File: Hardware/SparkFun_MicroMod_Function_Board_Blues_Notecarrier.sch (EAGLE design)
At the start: 3 parts, among them J1 MICROMOD_FUNCTION_STANDARD, U1 NOTECARD

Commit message: Board nearly complete, nearing readiness for design review.
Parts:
- added ANT_PWR, WP: JUMPER-SMT_2_NO_SILK, SparkFun-Jumpers:JUMPER-SMT_2_NO_SILK
- added AUX_EN_LED, USB_SHLD, VIO_LED, VMODEM_LED: JUMPER-SMT_2_NC_TRACE_SILK, SparkFun-Jumpers:JUMPER-SMT_2_NC_TRACE_SILK
- added C1, C5, C6, C7: 0.1uF, SparkFun-Capacitors:0.1UF-0402T-16V-10%
- added C2: 10uF, SparkFun-Capacitors:10UF-0805-10V-10%
- added C3, C4: 100uF, SparkFun-Capacitors:100UF-POLAR-25V-20%(ELEC)
- added C8: 1.0uF, SparkFun-Capacitors:1.0UF-0402T-16V-10%
- added D1, D2: RED, SparkFun-LED:LED-RED0603
- added D3: BLUE, SparkFun-LED:LED-BLUE0603
- added D4: PRTR5V0U2F, SparkFun-IC-Power:PRTR5V0U2F
- added D5, D6: 3A/10V/280mV, SparkFun-DiscreteSemi:DIODE-SCHOTTKY-BAT60A
- added D7: 0.5A/40V/420mV, SparkFun-DiscreteSemi:DIODE-SCHOTTKY-PMEG4005EJ
- added FD1, FD2, FD3, FD4: FIDUCIALUFIDUCIAL, SparkFun-Aesthetics:FIDUCIALUFIDUCIAL
- added H1: STAND-OFF-REFLOW-M2.5_2.5MM_TALL, SparkFun-Hardware:STAND-OFF-REFLOW-M2.5_2.5MM_TALL
- added J2: MICROMOD_FUNCTION_STANDARD, SparkFun-MicroMod:MICROMOD_FUNCTION_STANDARD
- added J3: (no value), SparkFun-Connectors:CONN_01PTH_NO_SILK_YES_STOP
- added J4: (no value), SparkFun-Connectors:CONN_07NO_SILK
- added J5: (no value), SparkFun-Connectors:SIMHOLDER-NANOSIM-MOLEX
- added J6: NOTECARD, SparkFun_MicroMod_Function_Board_Blues_Notecarrier:NOTECARD
- added LOGO1: SFE_LOGO_NAME_FLAME.1_INCH, SparkFun-Aesthetics:SFE_LOGO_NAME_FLAME.1_INCH
- added LOGO2: SPECIAL_INSTRUCTIONS-ORDERING, SparkFun-Aesthetics:SPECIAL_INSTRUCTIONS-ORDERING
- added LOGO3: OSHW-LOGOMINI, SparkFun-Aesthetics:OSHW-LOGOMINI
- added MEAS: JUMPER-COMBO_2_NC_TRACE, SparkFun-Jumpers:JUMPER-COMBO_2_NC_TRACE
- added Q1, Q3: 5.8A/30V/35mΩ, SparkFun-DiscreteSemi:MOSFET-NCH-AO3404A
- added Q2, Q4: 20V/4.2A/52mΩ/1.4W, SparkFun-DiscreteSemi:MOSFET_PCH-DMG2305UX-7
- added R1, R2: 1k, SparkFun-Resistors:1KOHM-0402T-1/16W-1%
- added R10, R11, R13, R5, R7, R9: 10k, SparkFun-Resistors:10KOHM-0402T-1/16W-1%
- added R12: 2.2M, SparkFun-Resistors:2.2MOHMS-0402T-1/10W-1%
- added R3, R4: 5.1k, SparkFun-Resistors:5.1KOHM-0402T-1/16W-1%
- added R6: 4.7k, SparkFun-Resistors:4.7KOHM-0402T-1/16W-1%
- added R8: 560Ω, SparkFun-Resistors:560OHM_0402_TIGHT
- added S1: MOMENTARY-SWITCH-SPST-SMD-4.6X2.8MM, SparkFun-Switches:MOMENTARY-SWITCH-SPST-SMD-4.6X2.8MM
- added U2: TCR2EF33, SparkFun_MicroMod_Function_Board_Blues_Notecarrier:TCR2EF33
- J1: value MICROMOD_FUNCTION_STANDARD -> (none); device SparkFun-MicroMod:MICROMOD_FUNCTION_STANDARD -> SparkFun-Connectors:USB_C_2-LAYER_PADS
- U1: value NOTECARD -> EEPROM; device SparkFun_MicroMod_Function_Board_Blues_Notecarrier:NOTECARD -> SparkFun-IC-Memory:EEPROM-I2C512K
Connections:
- new net !RESET!: J3.1, J6.!RST!, S1.2
- new net 3.3V: C1.1, C7.1, D1.A, D7.C, J6.VIO, Q2.D, R10.1, R5.1, U1.VCC
- new net 3V3_IN: J2.3.3V, Q2.S, R7.1, R9.2
- new net A0: J2.EEPROM_A0, U1.A0
- new net A1: J2.EEPROM_A1, U1.A1
- new net A2: J2.EEPROM_A2, U1.A2
- new net ATTN: J2.F3, J6.ATTN
- new net AUX1/MCU_!DFU_STAT!: J2.MCU_!DFU_STAT!, J4.6, J6.AUX1
- new net AUX2: J2.F5, J4.5, J6.AUX2
- new net AUX3/MCU_!BOOT!: J2.MCU_!BOOT!, J4.4, J6.AUX3
- new net AUX4/MCU_!RST!: J2.MCU_!RST!, J4.3, J6.AUX4
- new net AUX5: J2.F6, J4.7, J6.AUX5
- new net AUX_EN: D3.A, J2.F4, J4.2, J6.AUX_EN, R10.2
- new net AUX_RX/MCU_TX: J2.MCU_DFU_TX, J6.AUX_RX
- new net AUX_TX/MCU_RX: J2.MCU_DFU_RX, J6.AUX_TX
- new net EWP: J2.EEPROM_WP, R5.2, U1.WP, WP.2
- new net GND: AUX_EN_LED.1, C1.2, C2.2, C3.-, C4.-, C5.2, C6.2, C7.2, C8.2, D4.2, H1.1, J1.GND, J2.GND, J4.1, J5.GND, J6.GND, Q1.S, Q3.S, R12.1, R3.1, R4.1, S1.1, U1.GND, U2.GND, USB_SHLD.1, VIO_LED.1, VMODEM_LED.1, WP.1
- new net N$1: J2.PWR_EN, R8.2
- new net N$10: C8.1, D7.A, U2.OUT
- new net N$11: R2.1, VMODEM_LED.2
- new net N$12: R1.1, VIO_LED.2
- new net N$13: D3.C, R6.2
- new net N$14: AUX_EN_LED.2, R6.1
- new net N$2: Q1.D, Q2.G, R9.1
- new net N$3: Q3.D, Q4.G, R11.1
- new net N$37: D5.C, D6.C, MEAS.1
- new net N$4: D1.C, R1.2
- new net N$5: R13.1, U2.EN
- new net N$6: D2.C, R2.2
- new net N$8: J1.CC2, R3.2
- new net N$9: J1.CC1, R4.2
- new net NOTECARD_RX: J2.TX, J6.RX
- new net NOTECARD_TX: J2.RX, J6.TX
- new net PWR_EN: Q1.G, Q3.G, R7.2, R8.1
- new net SCL: J2.I2C_SCL, J6.SCL, U1.SCL
- new net SDA: J2.I2C_SDA, J6.SDA, U1.SDA
- new net SHLD: J1.SHLD, USB_SHLD.2
- new net SIM_CLK: J5.CLK, J6.SIM_CLK
- new net SIM_IO: J5.I/O, J6.SIM_IO
- new net SIM_RST: J5.RST, J6.SIM_RST
- new net SIM_VCC: C2.1, J5.VCC, J6.SIM_VCC
- new net USB_IN_N: D4.3, J1.D-
- new net USB_IN_P: D4.1, J1.D+
- new net USB_N: D4.4, J6.USB_D-
- new net USB_P: D4.6, J6.USB_D+
- new net VACT_GPS_IN: ANT_PWR.2, J6.VACT_GPS_IN
- new net VACT_GPS_OUT: ANT_PWR.1, J6.V_ACT_GPS_OUT
- new net VCC: D6.A, Q4.D
- new net VCC_IN: J2.VCC, Q4.S, R11.2
- new net VIN: C3.+, C4.+, C6.1, D2.A, J6.VMODEM, MEAS.2, R12.2
- new net V_USB: C5.1, D4.5, D5.A, J1.VBUS, J6.VUSB, R13.2, U2.IN
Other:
- note added: "AUX IO Breakout"
- note added: "Blues Notecard"
- note added: "External Active Antenna Power"
- note added: "External VIO Power"
- note added: "MicroMod Function Connector"
- note added: "Power Conditioning"
- note added: "Power Control"
- note added: "Power Indication"
- note added: "Reset Button and Breakout"
- note added: "SIM Card"
- note added: "USB Input"

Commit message: Board routing complete.
Initial routing complete, now finishing silk.
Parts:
- added D8: 0.5A/40V/420mV, SparkFun-DiscreteSemi:DIODE-SCHOTTKY-PMEG4005EJ
- J4: device SparkFun-Connectors:CONN_07NO_SILK -> SparkFun-Connectors:CONN_06NO_SILK_NO_POP
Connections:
- removed net AUX5: J2.F6, J4.7, J6.AUX5
- new net N$7: D8.A, Q2.D
- net 3.3V: now also D8.C; no longer Q2.D
- net VIN: now also C5.1, R13.2, U2.IN
- net V_USB: no longer C5.1, R13.2, U2.IN

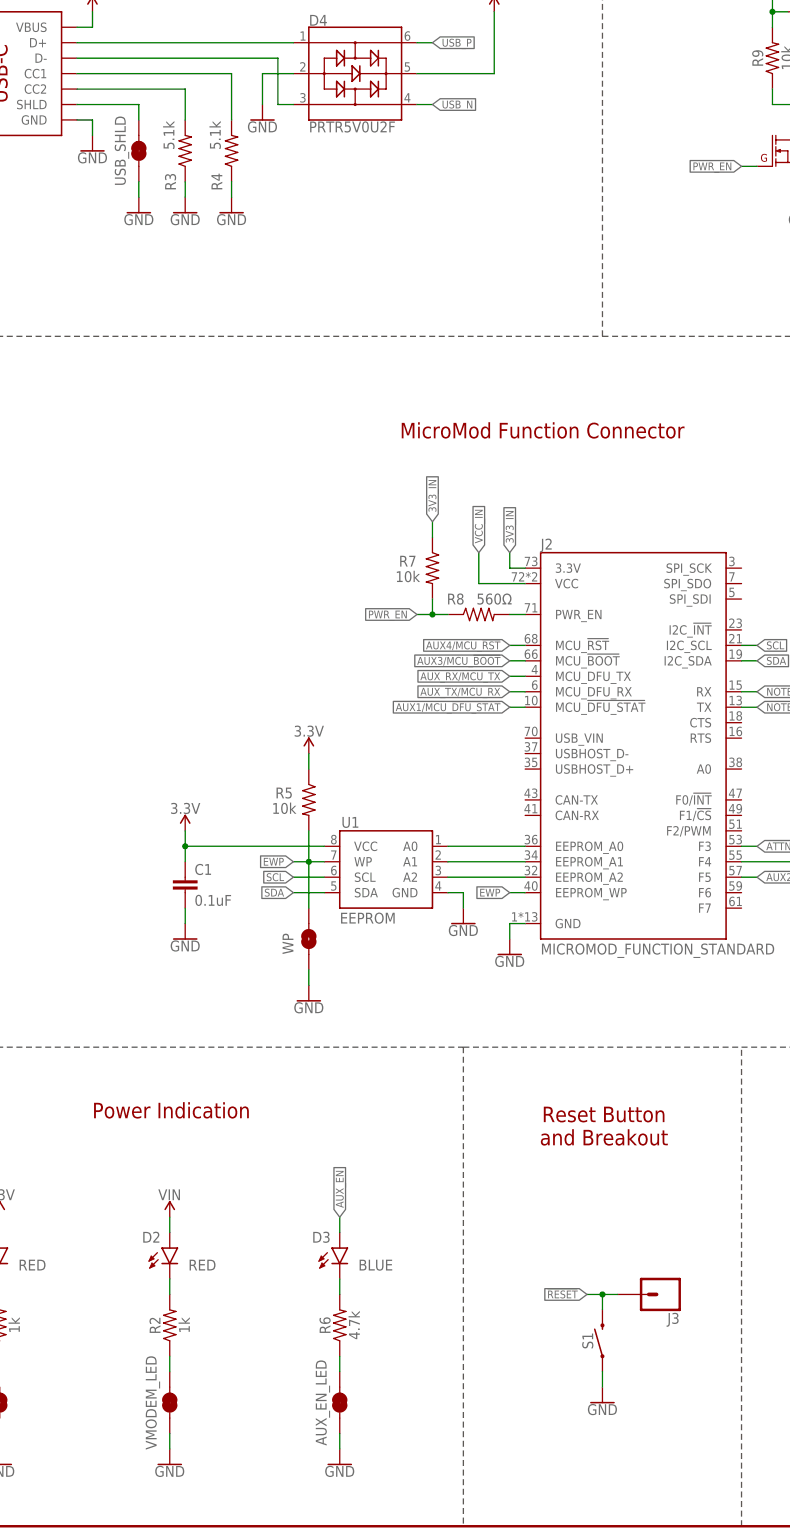
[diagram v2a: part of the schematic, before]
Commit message: Initial Silk completed.
May add Blues Wireless logo.
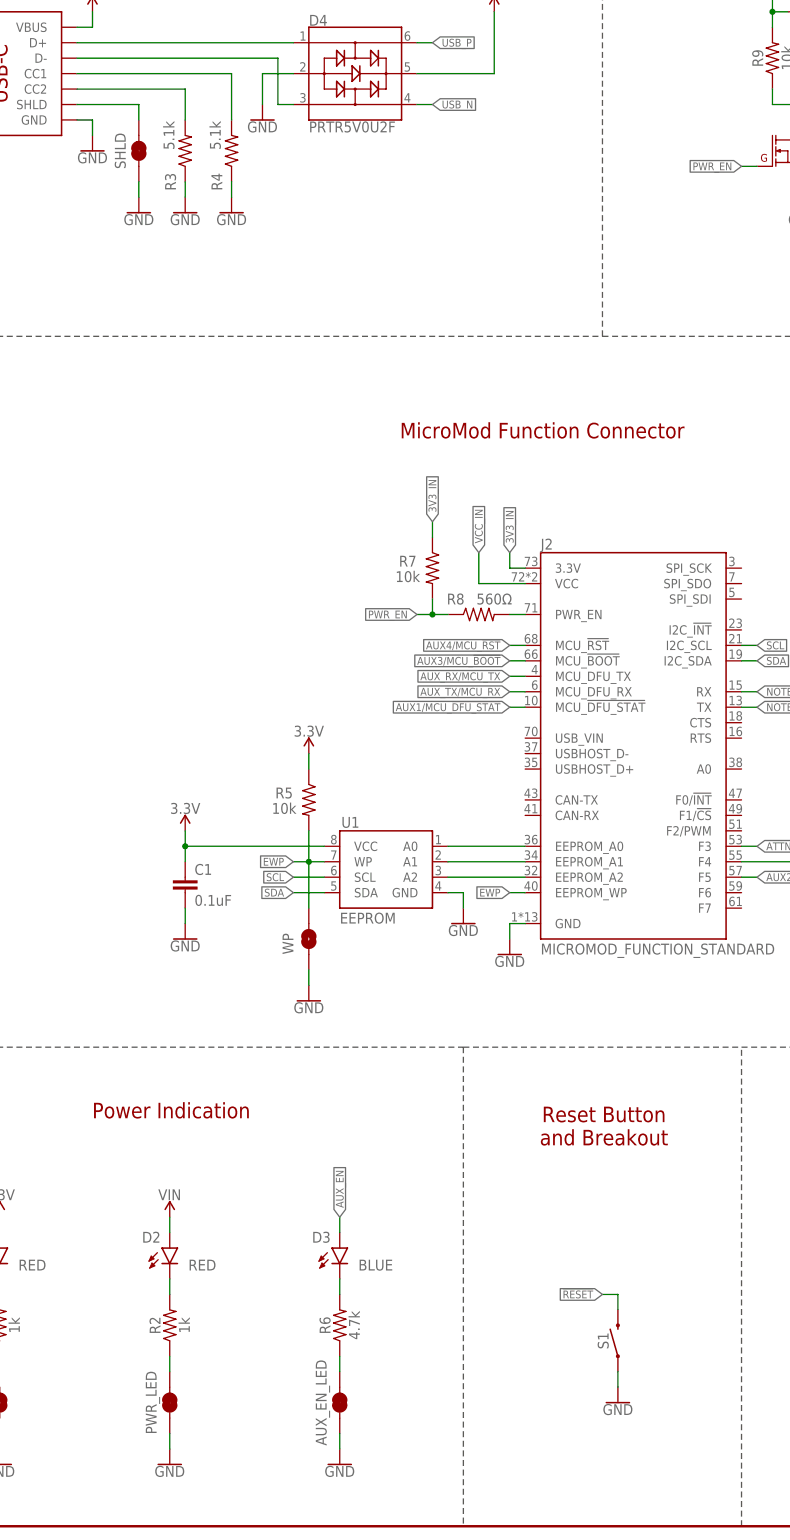
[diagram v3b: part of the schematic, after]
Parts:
- removed J3: (no value), SparkFun-Connectors:CONN_01PTH_NO_SILK_YES_STOP
- renumbered USB_SHLD to SHLD, VMODEM_LED to PWR_LED
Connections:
- net !RESET!: no longer J3.1
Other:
- moved on the sheet: S1
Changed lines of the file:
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@@
 <setting verticaltext="up"/>
 </settings>
-<grid distance="0.1" unitdist="inch" unit="inch" style="lines" multiple="1" display="no" altdistance="0.01" altunitdist="inch" altunit="inch"/>
+<grid distance="0.1" unitdist="inch" unit="inch" style="lines" multiple="1" display="yes" altdistance="0.01" altunitdist="inch" altunit="inch"/>
 <layers>
 <layer number="1" name="Top" color="4" fill="1" visible="no" active="no"/>
@@
 <part name="SUPPLY4" library="SparkFun-PowerSymbols" deviceset="V_USB" device=""/>
 <part name="SUPPLY5" library="SparkFun-PowerSymbols" deviceset="V_USB" device=""/>
-<part name="USB_SHLD" library="SparkFun-Jumpers" deviceset="JUMPER-SMT_2_NC_TRACE" device="_SILK" package3d_urn="urn:adsk.eagle:package:39281/1"/>
+<part name="SHLD" library="SparkFun-Jumpers" deviceset="JUMPER-SMT_2_NC_TRACE" device="_SILK" package3d_urn="urn:adsk.eagle:package:39281/1"/>
 <part name="R3" library="SparkFun-Resistors" deviceset="5.1KOHM" device="-0402T-1/16W-1%" value="5.1k"/>
 <part name="R4" library="SparkFun-Resistors" deviceset="5.1KOHM" device="-0402T-1/16W-1%" value="5.1k"/>
@@
 <part name="R2" library="SparkFun-Resistors" deviceset="1KOHM" device="-0402T-1/16W-1%" value="1k"/>
 <part name="VIO_LED" library="SparkFun-Jumpers" deviceset="JUMPER-SMT_2_NC_TRACE" device="_SILK" package3d_urn="urn:adsk.eagle:package:39281/1"/>
-<part name="VMODEM_LED" library="SparkFun-Jumpers" deviceset="JUMPER-SMT_2_NC_TRACE" device="_SILK" package3d_urn="urn:adsk.eagle:package:39281/1"/>
+<part name="PWR_LED" library="SparkFun-Jumpers" deviceset="JUMPER-SMT_2_NC_TRACE" device="_SILK" package3d_urn="urn:adsk.eagle:package:39281/1"/>
 <part name="GND23" library="SparkFun-PowerSymbols" deviceset="GND" device=""/>
 <part name="GND24" library="SparkFun-PowerSymbols" deviceset="GND" device=""/>
 <part name="SUPPLY16" library="SparkFun-PowerSymbols" deviceset="3.3V" device=""/>
 <part name="GND25" library="SparkFun-PowerSymbols" deviceset="GND" device=""/>
-<part name="J3" library="SparkFun-Connectors" deviceset="CONN_01" device="PTH_NO_SILK_YES_STOP"/>
 <part name="D3" library="SparkFun-LED" deviceset="LED-BLUE" device="0603" value="BLUE"/>
 <part name="R6" library="SparkFun-Resistors" deviceset="4.7KOHM" device="-0402T-1/16W-1%" value="4.7k"/>
@@
 <attribute name="VALUE" x="33.02" y="251.714" size="1.778" layer="96" font="vector" align="bottom-center"/>
 </instance>
-<instance part="USB_SHLD" gate="G$1" x="40.64" y="226.06" smashed="yes" rot="R90">
+<instance part="SHLD" gate="G$1" x="40.64" y="226.06" smashed="yes" rot="R90">
 <attribute name="NAME" x="37.592" y="226.06" size="1.778" layer="95" font="vector" rot="R90" align="center"/>
 </instance>
@@
 <attribute name="VALUE" x="208.28" y="254.254" size="1.778" layer="96" font="vector" align="bottom-center"/>
 </instance>
-<instance part="S1" gate="G$1" x="116.84" y="30.48" smashed="yes" rot="R90">
-<attribute name="NAME" x="115.316" y="30.48" size="1.778" layer="95" font="vector" rot="R90" align="bottom-center"/>
-</instance>
-<instance part="GND12" gate="1" x="116.84" y="20.32" smashed="yes">
-<attribute name="VALUE" x="116.84" y="20.066" size="1.778" layer="96" font="vector" align="top-center"/>
+<instance part="S1" gate="G$1" x="119.38" y="30.48" smashed="yes" rot="R90">
+<attribute name="NAME" x="117.856" y="30.48" size="1.778" layer="95" font="vector" rot="R90" align="bottom-center"/>
+</instance>
+<instance part="GND12" gate="1" x="119.38" y="20.32" smashed="yes">
+<attribute name="VALUE" x="119.38" y="20.066" size="1.778" layer="96" font="vector" align="top-center"/>
 </instance>
 <instance part="H1" gate="G1" x="396.24" y="132.08" smashed="yes">
@@
 <attribute name="NAME" x="14.732" y="20.32" size="1.778" layer="95" font="vector" rot="R90" align="center"/>
 </instance>
-<instance part="VMODEM_LED" gate="G$1" x="45.72" y="20.32" smashed="yes" rot="R90">
+<instance part="PWR_LED" gate="G$1" x="45.72" y="20.32" smashed="yes" rot="R90">
 <attribute name="NAME" x="42.672" y="20.32" size="1.778" layer="95" font="vector" rot="R90" align="center"/>
 </instance>
@@
 <instance part="GND25" gate="1" x="167.64" y="20.32" smashed="yes">
 <attribute name="VALUE" x="167.64" y="20.066" size="1.778" layer="96" font="vector" align="top-center"/>
-</instance>
-<instance part="J3" gate="G$1" x="127" y="38.1" smashed="yes" rot="R180">
-<attribute name="VALUE" x="129.54" y="42.926" size="1.778" layer="96" font="vector" rot="R180"/>
-<attribute name="NAME" x="129.54" y="35.052" size="1.778" layer="95" font="vector" rot="R180"/>
 </instance>
 <instance part="D3" gate="G$1" x="73.66" y="45.72" smashed="yes">
@@
 </segment>
 <segment>
-<pinref part="USB_SHLD" gate="G$1" pin="1"/>
+<pinref part="SHLD" gate="G$1" pin="1"/>
 <wire x1="40.64" y1="220.98" x2="40.64" y2="218.44" width="0.1524" layer="91"/>
 <pinref part="GND5" gate="1" pin="GND"/>
@@
 <segment>
 <pinref part="S1" gate="G$1" pin="1"/>
-<wire x1="116.84" y1="25.4" x2="116.84" y2="22.86" width="0.1524" layer="91"/>
+<wire x1="119.38" y1="25.4" x2="119.38" y2="22.86" width="0.1524" layer="91"/>
 <pinref part="GND12" gate="1" pin="GND"/>
 </segment>
@@
 </segment>
 <segment>
-<pinref part="VMODEM_LED" gate="G$1" pin="1"/>
+<pinref part="PWR_LED" gate="G$1" pin="1"/>
 <pinref part="GND24" gate="1" pin="GND"/>
 <wire x1="45.72" y1="15.24" x2="45.72" y2="12.7" width="0.1524" layer="91"/>
@@
 <wire x1="30.48" y1="233.68" x2="40.64" y2="233.68" width="0.1524" layer="91"/>
 <wire x1="40.64" y1="233.68" x2="40.64" y2="231.14" width="0.1524" layer="91"/>
-<pinref part="USB_SHLD" gate="G$1" pin="2"/>
+<pinref part="SHLD" gate="G$1" pin="2"/>
 </segment>
 </net>
@@
 <segment>
 <pinref part="S1" gate="G$1" pin="2"/>
-<wire x1="114.3" y1="38.1" x2="116.84" y2="38.1" width="0.1524" layer="91"/>
-<wire x1="116.84" y1="38.1" x2="116.84" y2="35.56" width="0.1524" layer="91"/>
 <wire x1="116.84" y1="38.1" x2="119.38" y2="38.1" width="0.1524" layer="91"/>
-<junction x="116.84" y="38.1"/>
-<label x="114.3" y="38.1" size="1.27" layer="95" font="vector" rot="R180" xref="yes"/>
-<pinref part="J3" gate="G$1" pin="1"/>
+<wire x1="119.38" y1="38.1" x2="119.38" y2="35.56" width="0.1524" layer="91"/>
+<label x="116.84" y="38.1" size="1.27" layer="95" font="vector" rot="R180" xref="yes"/>
 </segment>
 <segment>
@@
 <segment>
 <pinref part="R2" gate="G$1" pin="1"/>
-<pinref part="VMODEM_LED" gate="G$1" pin="2"/>
+<pinref part="PWR_LED" gate="G$1" pin="2"/>
 <wire x1="45.72" y1="27.94" x2="45.72" y2="25.4" width="0.1524" layer="91"/>
 </segment>

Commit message: Post DR updates.
Schematic:
Add Text to VREG
Add Text to Notecard
add 100 ohm resistor on pwr ctrl
Change Q1/Q3 transistors
Add Text to jumpers
Move V_USB on Notecard

Board:
Remove L2/L15
Add units for measures
Remove underscores from Silks
Move EWP via over
Remove copper layer notes
Give silk labels correct pointers
Increase mask stop on pads to ensure isolation
Move V_USB via down to allow ground pour
Check Wire stubs
Move 3.3V up to pour gnd better
Redo measures to make them look nice
Move some vias around to pour ground better
Place 100 ohm resistors
Place InRush current limiting resistor
Reroute
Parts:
- added R14, R15: 100, SparkFun-Resistors:100OHM-0402-TIGHT-1/16W-1%
- added R16: 1, SparkFun-Resistors:1OHM-0603-1/10W-1%
- Q1, Q3: value 5.8A/30V/35mΩ -> 220mA/50V/3.5Ω; device SparkFun-DiscreteSemi:MOSFET-NCH-AO3404A -> SparkFun-DiscreteSemi:MOSFET-NCH-BSS138
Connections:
- new net N$15: Q1.D, R14.1
- new net N$16: Q3.D, R15.1
- new net N$17: MEAS.2, R16.1
- net N$2: now also R14.2; no longer Q1.D
- net N$3: now also R15.2; no longer Q3.D
- net VIN: now also R16.2; no longer MEAS.2
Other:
- note added: "200mA out 5.5V max in"
- note added: "Connect to enable power for an active antenna. Default: Normally Open"
- note added: "Cut LED jumper to disable LED"
- note added: "Cut trace to measure current"
- note added: "USBSHLD Jumper Use this jumper to connect/disconnect your USB-C cable shield to this PCB's GND. Closed (default): connected to GND"
- note added: "VMODEM: 2.5 - 5.5V, 750mA continuous, 2A for < 20ms peak VIO: 3.3V, 150mA"
- moved on the sheet: C3, C4, C6, C7, D5, D6, H1, J6, MEAS, Q1, Q3, R12

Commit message: Update to v02.
Remove 10k PUR on AUX_EN
Add P-ch FET switch to AUX_EN
Rear Silk
Add Notecard SVG to silk
Change Title of Reset Section of Schematic
Reduce value of AEN LED bias resistor
Change FC symbol DFU pins to be named FC-centric
Add RGB neopixel and connect to AUX2
Add User Button and connect to AUX1
Add power gating FET for neopixel and connect to AUX3
Change AUX breakout
Swap UART RX/TX to match new FC symbol
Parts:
- removed J4: (no value), SparkFun-Connectors:CONN_06NO_SILK_NO_POP
- added C10: 0.1uF, SparkFun-Capacitors:0.1UF-0402T-16V-10%
- added C9: 1.0uF, SparkFun-Capacitors:1.0UF-0402T-16V-10%
- added D10: WS2812_2020, SparkFun-LED:WS2812_2020
- added D9: SMBJP6KE6.8A-TP, SparkFun_MicroMod_Function_Board_Blues_Notecarrier:SMBJP6KE6.8A-TP
- added J3: (no value), SparkFun-Connectors:CONN_041X04_NO_SILK_NO_POP
- added Q5: 220mA/50V/3.5Ω, SparkFun-DiscreteSemi:MOSFET-NCH-BSS138
- added Q6: 20V/4.2A/52mΩ/1.4W, SparkFun-DiscreteSemi:MOSFET_PCH-DMG2305UX-7
- added R17: 100, SparkFun-Resistors:100OHM-0402-TIGHT-1/16W-1%
- added RGB: JUMPER-SMT_2_NC_TRACE_SILK, SparkFun-Jumpers:JUMPER-SMT_2_NC_TRACE_SILK
- R6: value 4.7k -> 2.2k; device SparkFun-Resistors:4.7KOHM-0402T-1/16W-1% -> SparkFun-Resistors:2.2KOHM-0402T-1/16W-1%
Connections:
- removed net !RESET!: J6.!RST!, S1.2
- removed net AUX1/MCU_!DFU_STAT!: J2.MCU_!DFU_STAT!, J4.6, J6.AUX1
- removed net AUX2: J2.F5, J4.5, J6.AUX2
- removed net AUX3/MCU_!BOOT!: J2.MCU_!BOOT!, J4.4, J6.AUX3
- removed net AUX4/MCU_!RST!: J2.MCU_!RST!, J4.3, J6.AUX4
- new net AUX1/DFU_!ACTIVE!/USR_BTN: C9.1, D9.C, J2.DFU_!ACTIVE!, J6.AUX1, S1.2
- new net AUX2/RGB: D10.DI, J2.F5, J6.AUX2
- new net AUX3/DFU_!BOOT!: J2.DFU_!BOOT!, J6.AUX3
- new net AUX4/DFU_!RST!: J2.DFU_!RST!, J6.AUX4
- new net AUX_PWR: J2.F4, Q5.G
- new net N$18: C10.1, D10.VCC, RGB.1
- new net N$19: Q6.G, R10.1, R17.2
- new net N$20: Q5.D, R17.1
- net 3.3V: now also Q6.S, R10.2, RGB.2; no longer R10.1
- net AUX_EN: now also J3.4, Q6.D; no longer J2.F4, J4.2, R10.2
- net AUX_RX/MCU_TX: now also J2.DFU_FC_RX, J3.3; no longer J2.MCU_DFU_TX
- net AUX_TX/MCU_RX: now also J2.DFU_FC_TX, J3.2; no longer J2.MCU_DFU_RX
- net GND: now also C10.2, C9.2, D10.GND, D9.A, J3.1, Q5.S; no longer J4.1
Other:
- note added: "AUX UART Breakout"
- note added: "Cut RGB jumper to disable RGB LED"
- note added: "RGB LED"
- note added: "User Button"
- note added: "v02"
- note removed: "AUX IO Breakout"
- note removed: "Reset Button and Breakout"
- note removed: "v01"
- moved on the sheet: ANT_PWR, AUX_EN_LED, C1, C2, D1, D2, D3, J2, J5, PWR_LED, R1, R10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
